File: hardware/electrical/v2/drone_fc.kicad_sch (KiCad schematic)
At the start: 15 parts, among them J1 ESC_4IN1_JST_SH, J2 USB-C, J3 Cortex_SWD_10P, U1 MDBT53_P1M, U2 ICM-42688-P, U3 LMR50410_Buck

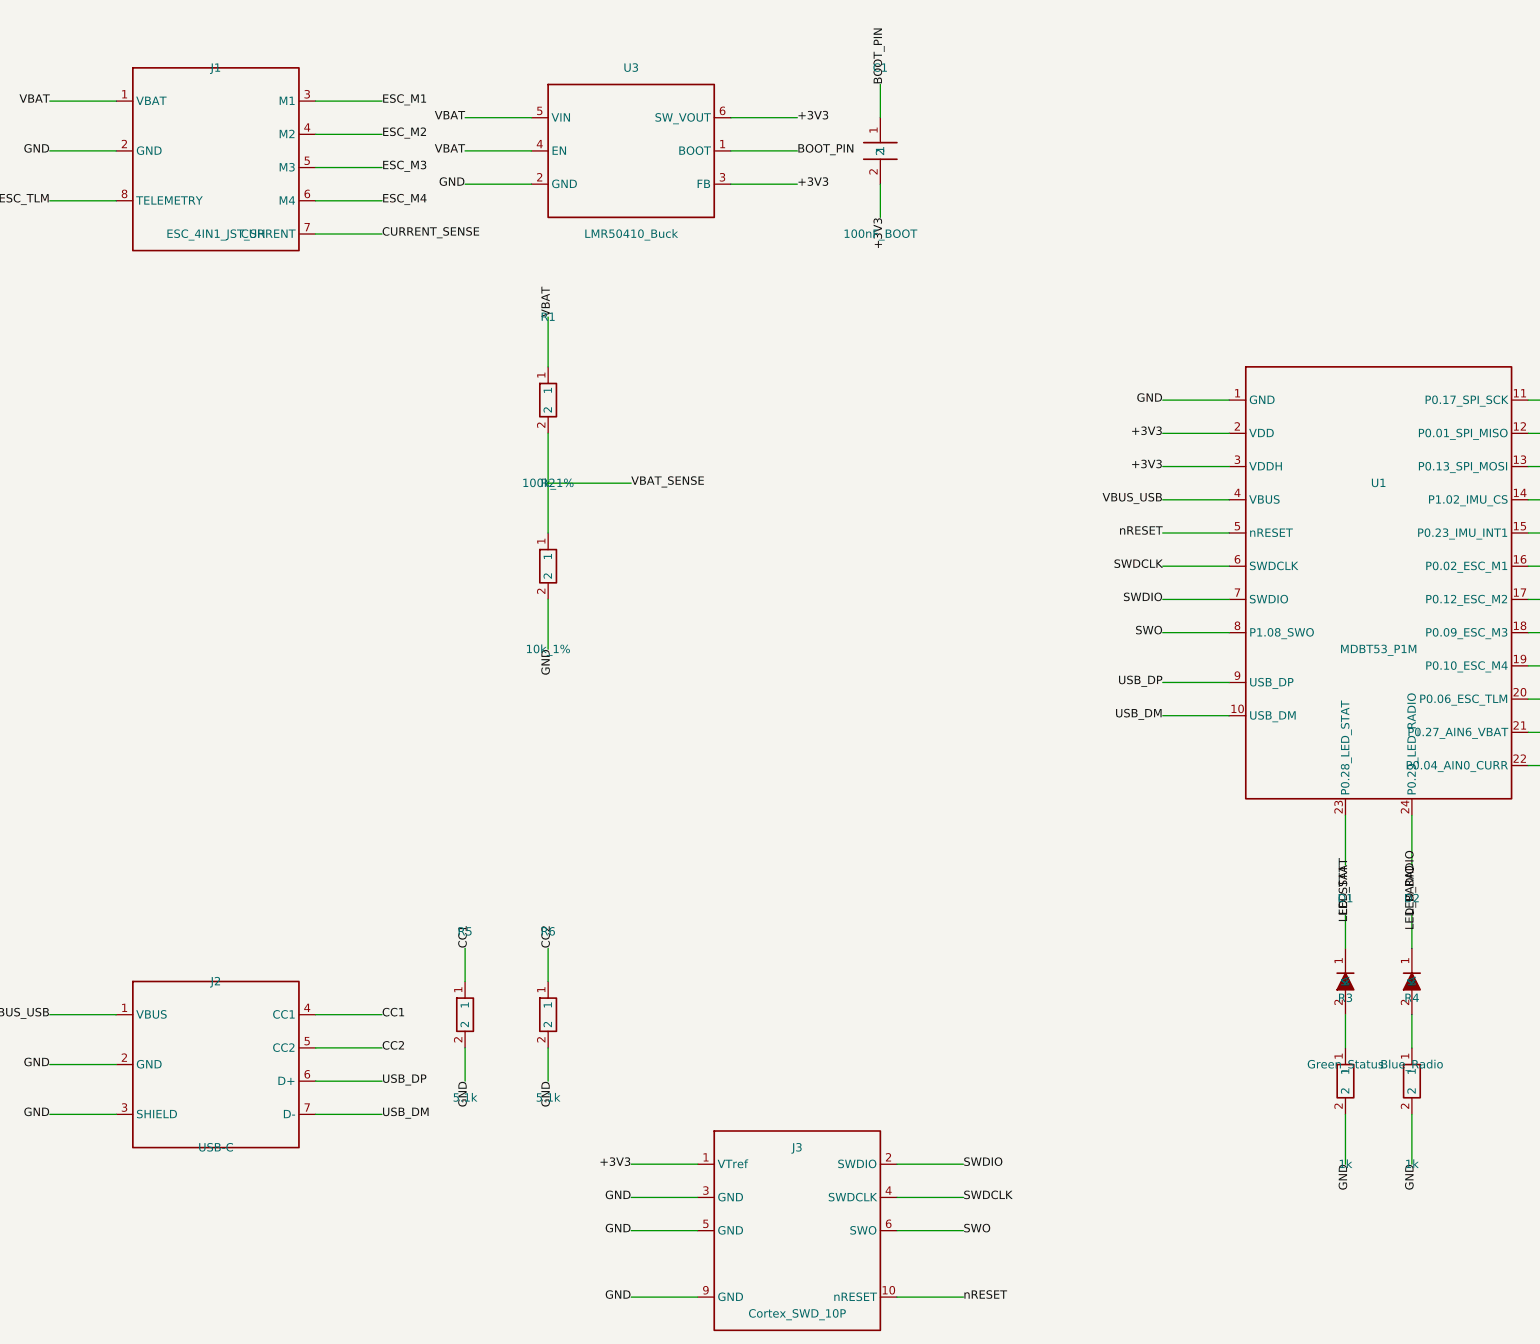
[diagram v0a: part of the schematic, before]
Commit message: hardware: update v2 flight-controller schematic and symbols
Work-in-progress edits to the nRF5340 carrier schematic (ADR 0026).
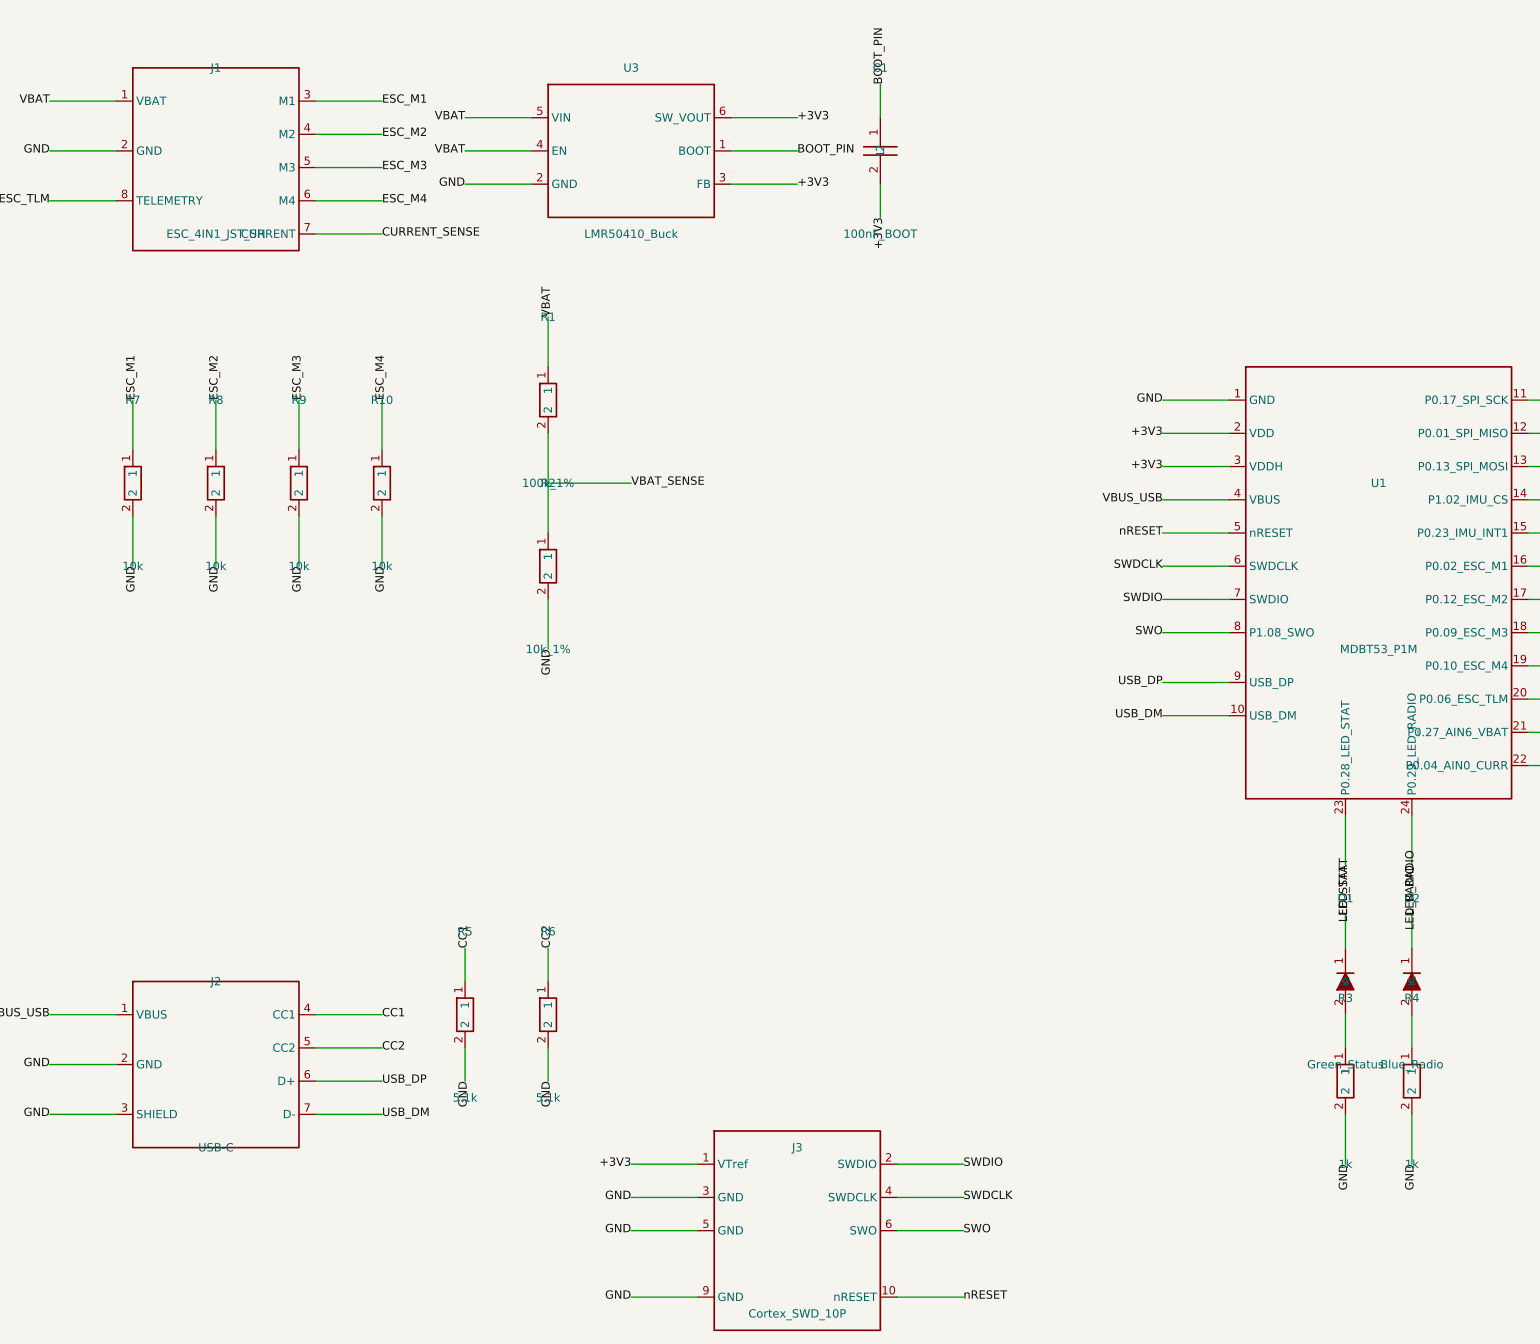
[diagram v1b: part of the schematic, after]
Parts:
- added R10, R7, R8, R9: 10k, symbol drone_fc_v2_symbols:Resistor
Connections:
- net ESC_M1: now also R7.1
- net ESC_M2: now also R8.1
- net ESC_M3: now also R9.1
- net ESC_M4: now also R10.1
- net GND: now also R10.2, R7.2, R8.2, R9.2

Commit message: power: add second-stage LDO (U4 TLV75533PDBVR) to two-stage regulation
Restores the agreed-upon power architecture (ADR 0025):
VBAT (via TVS1) → LMR50410 buck (U3) → +5V intermediate
+5V → TLV75533 LDO (U4) → +3V3 final rail

Added components:
- U4 TLV75533PDBVR (500 mA fixed 3.3V LDO, SOT-23-5)
- C9 (1µF 10V LDO input cap)
- C10 (1µF 6.3V LDO output cap)

Corrected buck output label from +3V3 to +5V intermediate.
Added explicit net labels at LDO input/output/ground endpoints.

Schematic renders successfully; ERC validation improved (44 → 35 violations).
Remaining ERC issues are CopperPilot regressions (USB, VBAT_SENSE, LED labels)
not power-stage connectivity problems.
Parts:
- removed J2: USB-C, symbol drone_fc_v2_symbols:USB_C_16Pin
- removed R5, R6: 5.1k, symbol drone_fc_v2_symbols:Resistor
- added C10: 1uF_6.3V_LDO_OUT, Capacitor_SMD:C_0603_1608Metric, symbol drone_fc_v2_symbols:Capacitor
- added C2: 10uF_50V, Capacitor_SMD:C_0805_2012Metric, symbol drone_fc_v2_symbols:Capacitor
- added C3: 22uF_10V, Capacitor_SMD:C_0805_2012Metric, symbol drone_fc_v2_symbols:Capacitor
- added C5, C7: 100nF, Capacitor_SMD:C_0402_1005Metric, symbol drone_fc_v2_symbols:Capacitor
- added C6: 10nF, Capacitor_SMD:C_0402_1005Metric, symbol drone_fc_v2_symbols:Capacitor
- added C8: 1uF, Capacitor_SMD:C_0402_1005Metric, symbol drone_fc_v2_symbols:Capacitor
- added C9: 1uF_10V_LDO_IN, Capacitor_SMD:C_0603_1608Metric, symbol drone_fc_v2_symbols:Capacitor
- added L1: 10uH, Inductor_SMD:L_0805_2012Metric, symbol drone_fc_v2_symbols:Inductor
- added R11: 43.2k_1%, Resistor_SMD:R_0402_1005Metric, symbol drone_fc_v2_symbols:Resistor
- added R12: 10k_1%, Resistor_SMD:R_0402_1005Metric, symbol drone_fc_v2_symbols:Resistor
- added TVS1: SMAJ24A, Diode_SMD:D_SMA, symbol drone_fc_v2_symbols:Diode_TVS
- added U4: TLV75533PDBVR, Package_TO_SOT_SMD:SOT-23-5, symbol drone_fc_v2_symbols:TLV75533PDBVR
- C1: footprint (none) -> Capacitor_SMD:C_0402_1005Metric
- D1, D2: footprint (none) -> LED_SMD:LED_0402_1005Metric
- J1: footprint (none) -> drone_fc_v2_footprints:JST_SH_SM08B-SRSS-TB_1x08-1MP_P1.00mm_Horizontal
- J3: footprint (none) -> Connector_PinHeader_1.27mm:PinHeader_2x05_P1.27mm_Vertical_SMD
- R1, R10, R2, R7, R8, R9: footprint (none) -> Resistor_SMD:R_0402_1005Metric
- R3, R4: value 1k -> 1k_1%; footprint (none) -> Resistor_SMD:R_0402_1005Metric
- U1: value MDBT53_P1M -> MDBT53-P1M; footprint (none) -> drone_fc_v2_footprints:MDBT53-P1M
- U2: footprint (none) -> drone_fc_v2_footprints:LGA-14_2.5x3.0mm_P0.5mm_ICM42688P
- U3: footprint (none) -> Package_TO_SOT_SMD:SOT-23-6
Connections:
- net +3V3: now also C10.1, C5.1, C6.1, C7.1, C8.1, U4.5 (OUT); no longer C1.2, U3.3 (FB), U3.6 (SW_VOUT)
- net CURRENT_SENSE: now also J1.6 (CURRENT); no longer J1.7 (CURRENT)
- net ESC_M1: now also J1.4 (M1), R7.2; no longer J1.3 (M1), R7.1
- net ESC_M2: now also J1.3 (M2), R8.2; no longer J1.4 (M2), R8.1
- net ESC_M3: now also J1.2 (M3), R9.2; no longer J1.5 (M3), R9.1
- net ESC_M4: now also J1.1 (M4), R10.2; no longer J1.6 (M4), R10.1
- net ESC_TLM: now also J1.5 (TELEMETRY); no longer J1.8 (TELEMETRY)
- net GND: now also J1.7 (GND), R10.1, R7.1, R8.1, R9.1, C10.2, C2.2, C3.2, C5.2, C6.2, C7.2, C8.2, C9.2, R12.2, TVS1.2 (A), U4.2 (GND); no longer J1.2 (GND), R10.2, R7.2, R8.2, R9.2
- net LED_RADIO: no longer D2.1 (A), U1.24 (P0.29_LED_RADIO)
- net LED_STAT: no longer D1.1 (A), U1.23 (P0.28_LED_STAT)
- net VBAT: now also J1.8 (VBAT), C2.1, TVS1.1 (K); no longer J1.1 (VBAT)
- net BOOT_PIN: no longer names the net of C1.1, U3.1 (BOOT)
- new net: C1.2, L1.1, U3.6 (SW)
- new net: D1.1 (A), U1.23 (P0.28_LED_STAT)
- new net: D2.1 (A), U1.24 (P0.29_LED_RADIO)
- new net: R11.2, R12.1, U3.3 (FB)
- new net +5V: C3.1, C9.1, L1.2, R11.1, U4.1 (IN)
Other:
- note added: "1. POWER REGULATION & VBAT SENSING"
- note added: "2. nRF5340 MCU CORE & 2.4GHz RF"
- note added: "3. ICM-42688-P 6-AXIS IMU"
- note added: "4. 4-IN-1 ESC INTERFACE & PULLDOWNS"
- note added: "5. SWD DEBUG INTERFACE"
- note added: "7. SYSTEM STATUS INDICATORS"

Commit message: schematic: clean battery sensing and power connectivity
Remove the redundant VBAT_SENSE resistor divider because battery voltage is supplied by ESC telemetry. Mark the unused MCU VBAT ADC pin no-connect and retain the explicit +5V power flag for the second-stage LDO input. Clean up stale wire and label warnings.
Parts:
- removed C7: 100nF, Capacitor_SMD:C_0402_1005Metric, symbol drone_fc_v2_symbols:Capacitor
- removed C8: 1uF, Capacitor_SMD:C_0402_1005Metric, symbol drone_fc_v2_symbols:Capacitor
- removed C9: 1uF_10V_LDO_IN, Capacitor_SMD:C_0603_1608Metric, symbol drone_fc_v2_symbols:Capacitor
- removed R1: 100k_1%, Resistor_SMD:R_0402_1005Metric, symbol drone_fc_v2_symbols:Resistor
- removed R2: 10k_1%, Resistor_SMD:R_0402_1005Metric, symbol drone_fc_v2_symbols:Resistor
- C10: value 1uF_6.3V_LDO_OUT -> 1uF
- L1: value 10uH -> 15uH
- R11: value 43.2k_1% -> 88.7K
- R12: value 10k_1% -> 22.1K
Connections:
- net ESC_M1: now also R10.1; no longer R7.2
- net ESC_M2: now also R9.1; no longer R8.2
- net ESC_M3: now also R8.1; no longer R9.2
- net ESC_M4: now also R7.1; no longer R10.2
- net GND: now also R10.2, R7.2, R8.2, R9.2; no longer R10.1, R7.1, R8.1, R9.1
- net at L1.1, U3.6 (SW): now also C1.1; no longer C1.2
- net at U3.1 (BOOT): now also C1.2; no longer C1.1
- net USB_DM: no longer names the net of U1.10 (USB_DM)
- net USB_DP: no longer names the net of U1.9 (USB_DP)
- net VBAT_SENSE: no longer names the net of U1.21 (P0.27_AIN6_VBAT)
- net VBUS_USB: no longer names the net of U1.4 (VBUS)
- no-connect marks 0 -> 4
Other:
- note added: "1. POWER REGULATION"
- note removed: "1. POWER REGULATION & VBAT SENSING"
- moved on the sheet: C1, C10, C2, C3, J3, L1, R10, R11, R12, R7, R8, R9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

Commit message: schematic: add MCU decoupling, IMU CS pull-up and INT2 pin
Drops the analog CURRENT_SENSE net: the ESC reports pack current over its serial telemetry, so a second path to the same shunt earned nothing and cost an ADC pin. J1 pin 6 and the MCU ADC pin are marked no-connect. Adds decoupling the module supply was missing entirely (4.7 uF bulk plus 100 nF per rail), a 1 uF local input cap at the LDO, and a 10k pull-up on IMU_CS so the IMU does not see spurious SPI while the MCU is in reset. Adds the missing INT2 pin 14 to the ICM-42688-P symbol, which is a 14-pad part, and marks it no-connect. ERC is clean: 0 errors, remaining warnings are library sync only. PCB layout is still work in progress and has known DRC violations.
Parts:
- added C11: 1uF, Capacitor_SMD:C_0603_1608Metric, symbol drone_fc_v2_symbols:Capacitor
- added C12, C13: 100nF, Capacitor_SMD:C_0805_2012Metric, symbol drone_fc_v2_symbols:Capacitor
- added C4: 4.7uF, Capacitor_SMD:C_0805_2012Metric, symbol drone_fc_v2_symbols:Capacitor
- added R13: 10k, Resistor_SMD:R_0402_1005Metric, symbol drone_fc_v2_symbols:Resistor
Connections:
- net +3V3: now also C12.1, C13.1, C4.1, R13.1
- net +5V: now also C11.1
- net GND: now also C11.2, C12.2, C13.2, C4.2
- net IMU_CS: now also R13.2
- net CURRENT_SENSE: no longer names the net of U1.22 (P0.04_AIN0_CURR)
- net CURRENT_SENSE: no longer J1.6 (CURRENT)
- no-connect marks 4 -> 7
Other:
- moved on the sheet: C3

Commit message: esc: correct J1 pinout to the standard 4-in-1 order
The ESC connector symbol was numbered end-for-end reversed: pin 1 was M4 and pin 8 was VBAT. Built that way, harness pin 1 would have delivered up to 16.8 V from the 4S pack into P0.10, an MCU GPIO, and swapped GND and all four motor signals with it. Renumbered to the standard 8-pin 4-in-1 pinout: 1 VBAT, 2 GND, 3 current, 4 telemetry, 5-8 M1-M4. Pin positions and names are unchanged, so schematic wiring is untouched and only the pad mapping moves; the MCU end of every net is unaffected. Confirmed three ways: the industry-standard convention, the harness wire colours (red VBAT, black GND, yellow current, green telemetry, white motors), and the JST pin 1 position on the fitted connector. Records the pinout and the colour code in the parts list, with the reasoning that colours are viewpoint-independent and pad order is not; a mirrored view of the ESC caused one false conclusion while drawing this. Also numbers the JST footprint mounting tabs MP instead of 2, which had been silently bonding the connector shell to whatever pin 2 carried.

Refs ADR 0023, where reversed ESC leads inverted roll and pitch.
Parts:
- C10, C11: footprint Capacitor_SMD:C_0603_1608Metric -> Capacitor_SMD:C_0402_1005Metric
- C12, C13, C2, C3, C4: footprint Capacitor_SMD:C_0805_2012Metric -> Capacitor_SMD:C_0402_1005Metric
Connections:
- net ESC_M1: now also J1.5 (M1); no longer J1.4 (M1)
- net ESC_M2: now also J1.6 (M2); no longer J1.3 (M2)
- net ESC_M3: now also J1.7 (M3); no longer J1.2 (M3)
- net ESC_M4: now also J1.8 (M4); no longer J1.1 (M4)
- net ESC_TLM: now also J1.4 (TELEMETRY); no longer J1.5 (TELEMETRY)
- net GND: now also J1.2 (GND); no longer J1.7 (GND)
- net VBAT: now also J1.1 (VBAT); no longer J1.8 (VBAT)

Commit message: power: complete LDO symbol, drop rail to 4V, clean up library
U4 (TLV75533PDBVR) was missing EN and NC pins; EN floating would
have left the regulator in permanent shutdown. Symbol now has all
5 pins, EN wired to +5V (always-on), verified against
doc/hardware/tlv755p.pdf Table 4-1.

Lower R11 to 66.5K so the buck's intermediate rail is ~4.0V instead
of 5.0V, giving headroom against the LDO's 5.5V absolute max input
and roughly halving its dissipation.

Hide pin name/number text on discrete passives (R, C, L, LED, TVS
diode) in the library and schematic cache, matching stock KiCad
Device symbol convention. ICs and connectors keep pin labels shown.

Remove CopperPilot attribution from title blocks, and remove the
unused USBLC6_2SC6 / USB_C_16Pin symbols and footprint left over
from the earlier USB removal.
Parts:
- C1: value 100nF_BOOT -> 100nF
- R11: value 88.7K -> 66.5K
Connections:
- net +5V renamed +4V
- net +4V: now also U4.3 (EN)
